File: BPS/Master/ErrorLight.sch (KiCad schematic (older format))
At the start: 16 parts, among them J9 ErrorLightConnector, Q3 NTR4003NT1G, Q4 NTR4003NT1G, U14 SI8261ABC-IS

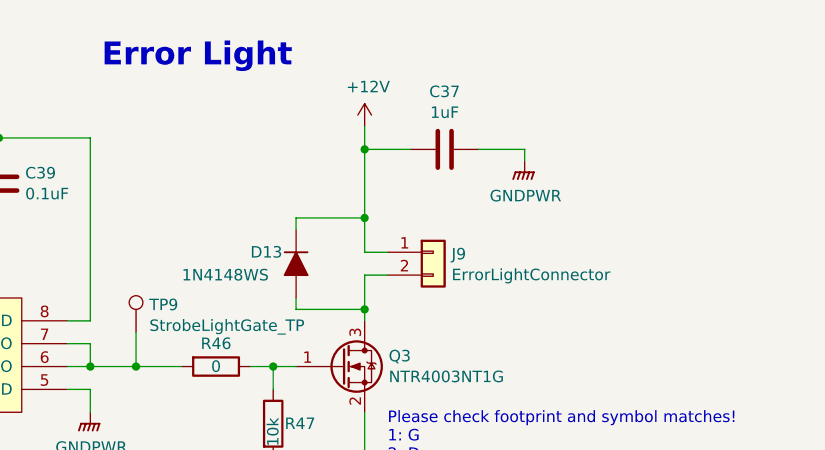
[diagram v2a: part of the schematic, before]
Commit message: Added button to change strobelight pulsing pattern.
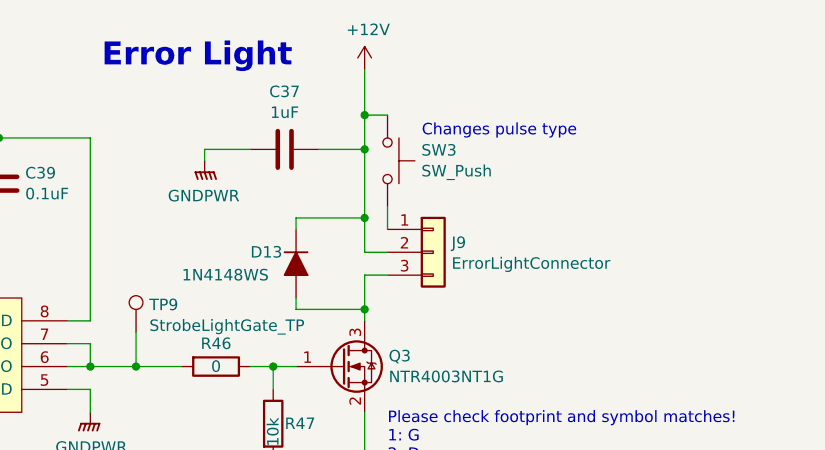
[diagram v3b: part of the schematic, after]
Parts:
- removed J9: ErrorLightConnector, UTSVT_Connectors:Molex_MicroFit3.0_1x2xP3.00mm_PolarizingPeg_Vertical, symbol Connector_Generic:Conn_01x02
- added J9: ErrorLightConnector, symbol Connector_Generic:Conn_01x03
- added SW3: SW_Push, symbol Switch:SW_Push
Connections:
- net +12V: now also J9.2 (Pin_2), SW3.1
- net at D13.2 (A), Q3.3 (D): now also J9.3 (Pin_3)
- new net: J9.1 (Pin_1), SW3.2
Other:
- note added: "Changes pulse type"
- moved on the sheet: C37
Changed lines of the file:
@@
 Comment4 ""
 $EndDescr
-$Comp
-L Connector_Generic:Conn_01x02 J?
-U 1 1 5D93093E
-P 7350 3450
-AR Path="/5C392C6A/5D93093E" Ref="J?"  Part="1"
-AR Path="/5D923D59/5D93093E" Ref="J9"  Part="1"
-F 0 "J9" H 7430 3442 50  0000 L CNN
-F 1 "ErrorLightConnector" H 7430 3351 50  0000 L CNN
-F 2 "UTSVT_Connectors:Molex_MicroFit3.0_1x2xP3.00mm_PolarizingPeg_Vertical" H 7350 3450 50  0001 C CNN
-F 3 "~" H 7350 3450 50  0001 C CNN
-	1    7350 3450
-	1    0    0    -1
-$EndComp
 Text Notes 5900 2650 0    100  ~ 20
 Error Light
@@
 L power:+12V #PWR?
 U 1 1 5D930982
-P 7050 2900
+P 7050 2650
 AR Path="/5C38C674/5D930982" Ref="#PWR?"  Part="1"
 AR Path="/5C392C6A/5D930982" Ref="#PWR?"  Part="1"
 AR Path="/5D923D59/5D930982" Ref="#PWR073"  Part="1"
-F 0 "#PWR073" H 7050 2750 50  0001 C CNN
-F 1 "+12V" H 7065 3073 50  0000 C CNN
-F 2 "" H 7050 2900 50  0001 C CNN
-F 3 "" H 7050 2900 50  0001 C CNN
-	1    7050 2900
+F 0 "#PWR073" H 7050 2500 50  0001 C CNN
+F 1 "+12V" H 7065 2823 50  0000 C CNN
+F 2 "" H 7050 2650 50  0001 C CNN
+F 3 "" H 7050 2650 50  0001 C CNN
+	1    7050 2650
 	1    0    0    -1
 $EndComp
@@
 L Device:C C?
 U 1 1 5D9309C2
-P 7400 3000
+P 6700 3000
 AR Path="/5C38C674/5D9309C2" Ref="C?"  Part="1"
 AR Path="/5C392C6A/5D9309C2" Ref="C?"  Part="1"
 AR Path="/5D923D59/5D9309C2" Ref="C37"  Part="1"
-F 0 "C37" V 7148 3000 50  0000 C CNN
-F 1 "1uF" V 7239 3000 50  0000 C CNN
-F 2 "Capacitor_SMD:C_0805_2012Metric" H 7438 2850 50  0001 C CNN
-F 3 "~" H 7400 3000 50  0001 C CNN
-	1    7400 3000
-	0    1    1    0
+F 0 "C37" V 6448 3000 50  0000 C CNN
+F 1 "1uF" V 6539 3000 50  0000 C CNN
+F 2 "Capacitor_SMD:C_0805_2012Metric" H 6738 2850 50  0001 C CNN
+F 3 "~" H 6700 3000 50  0001 C CNN
+	1    6700 3000
+	0    -1   1    0
 $EndComp
 $Comp
 L power:GNDPWR #PWR?
 U 1 1 5D9309C8
-P 7750 3050
+P 6350 3050
 AR Path="/5C38C674/5D9309C8" Ref="#PWR?"  Part="1"
 AR Path="/5C392C6A/5D9309C8" Ref="#PWR?"  Part="1"
 AR Path="/5D923D59/5D9309C8" Ref="#PWR074"  Part="1"
-F 0 "#PWR074" H 7750 2850 50  0001 C CNN
-F 1 "GNDPWR" H 7754 2896 50  0000 C CNN
-F 2 "" H 7750 3000 50  0001 C CNN
-F 3 "" H 7750 3000 50  0001 C CNN
-	1    7750 3050
-	1    0    0    -1
-$EndComp
-Wire Wire Line
-	7750 3050 7750 3000
-Wire Wire Line
-	7750 3000 7550 3000
-Wire Wire Line
-	7050 2900 7050 3000
-Wire Wire Line
-	7250 3000 7050 3000
+F 0 "#PWR074" H 6350 2850 50  0001 C CNN
+F 1 "GNDPWR" H 6354 2896 50  0000 C CNN
+F 2 "" H 6350 3000 50  0001 C CNN
+F 3 "" H 6350 3000 50  0001 C CNN
+	1    6350 3050
+	-1   0    0    -1
+$EndComp
+Wire Wire Line
+	6350 3050 6350 3000
+Wire Wire Line
+	6350 3000 6550 3000
+Wire Wire Line
+	6850 3000 7050 3000
 Connection ~ 7050 3000
 Wire Wire Line
@@
 Wire Wire Line
 	5850 3950 6050 3950
+$Comp
+L Connector_Generic:Conn_01x03 J9
+U 1 1 5EF1892A
+P 7350 3450
+F 0 "J9" H 7430 3492 50  0000 L CNN
+F 1 "ErrorLightConnector" H 7430 3401 50  0000 L CNN
+F 2 "" H 7350 3450 50  0001 C CNN
+F 3 "~" H 7350 3450 50  0001 C CNN
+	1    7350 3450
+	1    0    0    -1
+$EndComp
+Wire Wire Line
+	7150 3350 7150 3250
+$Comp
+L Switch:SW_Push SW3
+U 1 1 5EF1C7EF
+P 7150 3050
+F 0 "SW3" V 7104 3198 50  0000 L CNN
+F 1 "SW_Push" V 7195 3198 50  0000 L CNN
+F 2 "" H 7150 3250 50  0001 C CNN
+F 3 "~" H 7150 3250 50  0001 C CNN
+	1    7150 3050
+	0    1    1    0
+$EndComp
+Wire Wire Line
+	7050 2850 7150 2850
+Wire Wire Line
+	7050 2850 7050 3000
+Wire Wire Line
+	7050 2850 7050 2650
+Connection ~ 7050 2850
+Text Notes 7300 2950 0    50   ~ 0
+Changes pulse type
 $EndSCHEMATC

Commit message: Assigned footprints to all symbols except reset circuit(high voltage detector). Changed 18 pin connector to 3, 6 pin connectors. Generated netlist.
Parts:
- J9: footprint (none) -> UTSVT_Connectors:Molex_MicroFit3.0_1x3xP3.00mm_PolarizingPeg_Vertical
- SW3: footprint (none) -> Button_Switch_SMD:SW_SPST_B3SL-1002P
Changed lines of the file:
@@
 F 0 "J9" H 7430 3492 50  0000 L CNN
 F 1 "ErrorLightConnector" H 7430 3401 50  0000 L CNN
-F 2 "" H 7350 3450 50  0001 C CNN
+F 2 "UTSVT_Connectors:Molex_MicroFit3.0_1x3xP3.00mm_PolarizingPeg_Vertical" H 7350 3450 50  0001 C CNN
 F 3 "~" H 7350 3450 50  0001 C CNN
 	1    7350 3450
@@
 F 0 "SW3" V 7104 3198 50  0000 L CNN
 F 1 "SW_Push" V 7195 3198 50  0000 L CNN
-F 2 "" H 7150 3250 50  0001 C CNN
+F 2 "Button_Switch_SMD:SW_SPST_B3SL-1002P" H 7150 3250 50  0001 C CNN
 F 3 "~" H 7150 3250 50  0001 C CNN
 	1    7150 3050

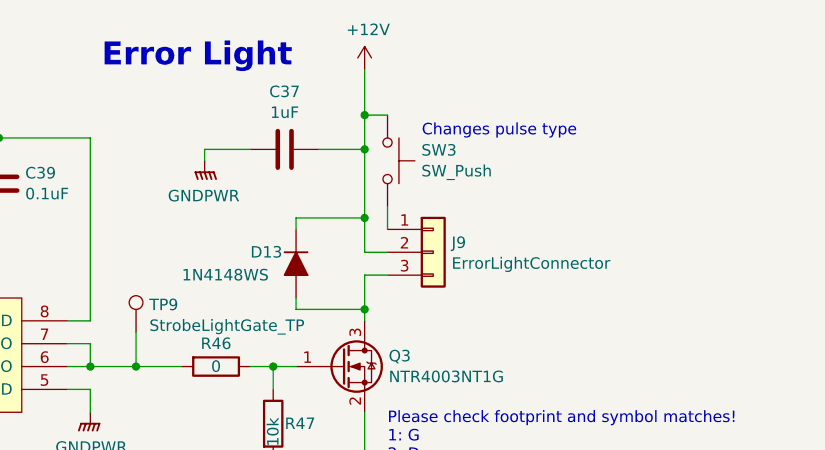
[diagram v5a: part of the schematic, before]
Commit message: Reverts edited files that are not related to the FanBoard back to master branch's versions
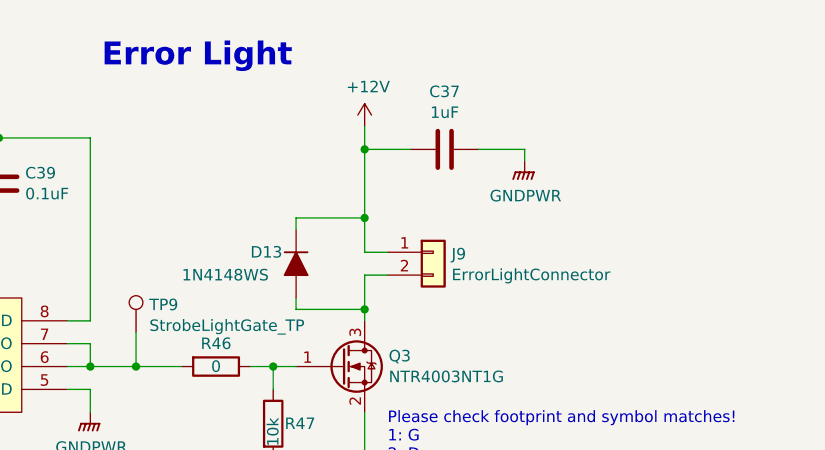
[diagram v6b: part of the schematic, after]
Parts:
- removed J9: ErrorLightConnector, UTSVT_Connectors:Molex_MicroFit3.0_1x3xP3.00mm_PolarizingPeg_Vertical, symbol Connector_Generic:Conn_01x03
- removed SW3: SW_Push, Button_Switch_SMD:SW_SPST_B3SL-1002P, symbol Switch:SW_Push
- added J9: ErrorLightConnector, UTSVT_Connectors:Molex_MicroFit3.0_1x2xP3.00mm_PolarizingPeg_Vertical, symbol Connector_Generic:Conn_01x02
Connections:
- net +12V: now also J9.1 (Pin_1)
- net at D13.2 (A), Q3.3 (D): now also J9.2 (Pin_2)
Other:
- note removed: "Changes pulse type"
- moved on the sheet: C37
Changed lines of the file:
@@
 $Descr A4 11693 8268
 encoding utf-8
-Sheet 8 10
+Sheet 9 10
 Title ""
 Date ""
@@
 Comment4 ""
 $EndDescr
+$Comp
+L Connector_Generic:Conn_01x02 J?
+U 1 1 5D93093E
+P 7350 3450
+AR Path="/5C392C6A/5D93093E" Ref="J?"  Part="1"
+AR Path="/5D923D59/5D93093E" Ref="J9"  Part="1"
+F 0 "J9" H 7430 3442 50  0000 L CNN
+F 1 "ErrorLightConnector" H 7430 3351 50  0000 L CNN
+F 2 "UTSVT_Connectors:Molex_MicroFit3.0_1x2xP3.00mm_PolarizingPeg_Vertical" H 7350 3450 50  0001 C CNN
+F 3 "~" H 7350 3450 50  0001 C CNN
+	1    7350 3450
+	1    0    0    -1
+$EndComp
 Text Notes 5900 2650 0    100  ~ 20
 Error Light
@@
 L power:+12V #PWR?
 U 1 1 5D930982
-P 7050 2650
+P 7050 2900
 AR Path="/5C38C674/5D930982" Ref="#PWR?"  Part="1"
 AR Path="/5C392C6A/5D930982" Ref="#PWR?"  Part="1"
 AR Path="/5D923D59/5D930982" Ref="#PWR073"  Part="1"
-F 0 "#PWR073" H 7050 2500 50  0001 C CNN
-F 1 "+12V" H 7065 2823 50  0000 C CNN
-F 2 "" H 7050 2650 50  0001 C CNN
-F 3 "" H 7050 2650 50  0001 C CNN
-	1    7050 2650
+F 0 "#PWR073" H 7050 2750 50  0001 C CNN
+F 1 "+12V" H 7065 3073 50  0000 C CNN
+F 2 "" H 7050 2900 50  0001 C CNN
+F 3 "" H 7050 2900 50  0001 C CNN
+	1    7050 2900
 	1    0    0    -1
 $EndComp
@@
 L Device:C C?
 U 1 1 5D9309C2
-P 6700 3000
+P 7400 3000
 AR Path="/5C38C674/5D9309C2" Ref="C?"  Part="1"
 AR Path="/5C392C6A/5D9309C2" Ref="C?"  Part="1"
 AR Path="/5D923D59/5D9309C2" Ref="C37"  Part="1"
-F 0 "C37" V 6448 3000 50  0000 C CNN
-F 1 "1uF" V 6539 3000 50  0000 C CNN
-F 2 "Capacitor_SMD:C_0805_2012Metric" H 6738 2850 50  0001 C CNN
-F 3 "~" H 6700 3000 50  0001 C CNN
-	1    6700 3000
-	0    -1   1    0
+F 0 "C37" V 7148 3000 50  0000 C CNN
+F 1 "1uF" V 7239 3000 50  0000 C CNN
+F 2 "Capacitor_SMD:C_0805_2012Metric" H 7438 2850 50  0001 C CNN
+F 3 "~" H 7400 3000 50  0001 C CNN
+	1    7400 3000
+	0    1    1    0
 $EndComp
 $Comp
 L power:GNDPWR #PWR?
 U 1 1 5D9309C8
-P 6350 3050
+P 7750 3050
 AR Path="/5C38C674/5D9309C8" Ref="#PWR?"  Part="1"
 AR Path="/5C392C6A/5D9309C8" Ref="#PWR?"  Part="1"
 AR Path="/5D923D59/5D9309C8" Ref="#PWR074"  Part="1"
-F 0 "#PWR074" H 6350 2850 50  0001 C CNN
-F 1 "GNDPWR" H 6354 2896 50  0000 C CNN
-F 2 "" H 6350 3000 50  0001 C CNN
-F 3 "" H 6350 3000 50  0001 C CNN
-	1    6350 3050
-	-1   0    0    -1
-$EndComp
-Wire Wire Line
-	6350 3050 6350 3000
-Wire Wire Line
-	6350 3000 6550 3000
-Wire Wire Line
-	6850 3000 7050 3000
+F 0 "#PWR074" H 7750 2850 50  0001 C CNN
+F 1 "GNDPWR" H 7754 2896 50  0000 C CNN
+F 2 "" H 7750 3000 50  0001 C CNN
+F 3 "" H 7750 3000 50  0001 C CNN
+	1    7750 3050
+	1    0    0    -1
+$EndComp
+Wire Wire Line
+	7750 3050 7750 3000
+Wire Wire Line
+	7750 3000 7550 3000
+Wire Wire Line
+	7050 2900 7050 3000
+Wire Wire Line
+	7250 3000 7050 3000
 Connection ~ 7050 3000
 Wire Wire Line
@@
 Wire Wire Line
 	5850 3950 6050 3950
-$Comp
-L Connector_Generic:Conn_01x03 J9
-U 1 1 5EF1892A
-P 7350 3450
-F 0 "J9" H 7430 3492 50  0000 L CNN
-F 1 "ErrorLightConnector" H 7430 3401 50  0000 L CNN
-F 2 "UTSVT_Connectors:Molex_MicroFit3.0_1x3xP3.00mm_PolarizingPeg_Vertical" H 7350 3450 50  0001 C CNN
-F 3 "~" H 7350 3450 50  0001 C CNN
-	1    7350 3450
-	1    0    0    -1
-$EndComp
-Wire Wire Line
-	7150 3350 7150 3250
-$Comp
-L Switch:SW_Push SW3
-U 1 1 5EF1C7EF
-P 7150 3050
-F 0 "SW3" V 7104 3198 50  0000 L CNN
-F 1 "SW_Push" V 7195 3198 50  0000 L CNN
-F 2 "Button_Switch_SMD:SW_SPST_B3SL-1002P" H 7150 3250 50  0001 C CNN
-F 3 "~" H 7150 3250 50  0001 C CNN
-	1    7150 3050
-	0    1    1    0
-$EndComp
-Wire Wire Line
-	7050 2850 7150 2850
-Wire Wire Line
-	7050 2850 7050 3000
-Wire Wire Line
-	7050 2850 7050 2650
-Connection ~ 7050 2850
-Text Notes 7300 2950 0    50   ~ 0
-Changes pulse type
 $EndSCHEMATC
